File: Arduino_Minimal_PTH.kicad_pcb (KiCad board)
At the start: 2 copper layers, 27.9 x 45.7 mm, 22 parts, among them IC1 ATMEGA328P-PU, P1 I/O lo, P2 FTDI Basic, P3 A4 A5, P4 I/O hi, SW1 Reset, U1 L4931CZ50-AP, X1 CSTLS16M0X53-B0

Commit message: Placed.
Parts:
- removed C1: 10u, mfk-CRP_5.0_2.0_0.5
- removed C3: 100n, mfk-C_4.0_2.5_2.5_0.5
- removed D1, D2: LED, LED-3MM
- removed R1: 10K, mfk-R_0.25W_RN55_vert
- removed R3: 330, mfk-R_0.25W_RN55_vert
- removed R4, R5: opt, mfk-R_0.25W_RN55_vert
- removed U1: L4931CZ50-AP, mfk-TO-92_f321
- removed VAL: REF, oshw-logo-150mil-FSilk
- C2: footprint mfk-CRP_5.0_2.0_0.5 -> mfk-CRP_4.0_2.5_0.5
- C4, C7, C8: moved to B.Cu
- SW1: footprint mfk-SW_PUSH_6MM -> mfk-SW_PUSH_6x3.5mm
- moved X1 26.2 mm to (129.2, 88.1)
- moved P3 14.2 mm to (143.5, 91.4)
- moved R2 12.9 mm to (133.6, 86.4), turned to 0 degrees
- moved C4 12.0 mm to (137.8, 86.4)
- moved SW1 9.47 mm to (135.8, 89.4)
- moved C7 7.62 mm to (135.9, 110.5), turned to 180 degrees
- moved C8 7.62 mm to (135.9, 108.0), turned to 0 degrees
- moved P1 5.08 mm to (128.3, 109.2)
- moved P4 5.08 mm to (143.5, 109.2)
- moved C2 4.36 mm to (142.4, 86.4), turned to 180 degrees
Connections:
- P4 pad 1: RAW -> (no net)
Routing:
- net GND: track 106.3 -> 0.00 mm, vias 1 -> 0
- net VCC: track 75.8 -> 0.00 mm, vias 1 -> 0
- net RESET: track 44.5 -> 0.00 mm
- net A3: track 37.1 -> 0.00 mm
- net TXO: track 32.9 -> 0.00 mm
- net RXI: track 24.9 -> 0.00 mm
- net DTR: track 18.1 -> 0.00 mm
- net D9: track 17.6 -> 0.00 mm
- net A2: track 14.2 -> 0.00 mm
- net A5: track 13.9 -> 0.00 mm
- net A4: track 13.9 -> 0.00 mm
- net A1: track 12.9 -> 0.00 mm
- net A0: track 12.2 -> 0.00 mm
- net D4: track 11.2 -> 0.00 mm
- net D6: track 11.0 -> 0.00 mm
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- removed copper zone on B.Cu, net GND
- removed copper zone on F.Cu, net GND
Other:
- board size 27.9 x 45.7 mm -> 17.8 x 45.7 mm
- board text added: "NC"
- board text added: "VCC"
- board text removed: "RAW"
- board text removed: "Reset"

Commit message: Routed
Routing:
- net GND: track 0.00 -> 71.8 mm
- net VCC: track 0.00 -> 62.8 mm, vias 0 -> 1
- net RESET: track 0.00 -> 36.4 mm
- net TXO: track 0.00 -> 30.9 mm, vias 0 -> 3
- net N-0000015: track 0.00 -> 28.6 mm
- net N-000005: track 0.00 -> 26.1 mm
- net RXI: track 0.00 -> 20.1 mm
- net D9: track 0.00 -> 12.5 mm
- net A0: track 0.00 -> 10.8 mm
- net A2: track 0.00 -> 9.20 mm
- net A1: track 0.00 -> 9.20 mm
- net A3: track 0.00 -> 9.20 mm
- net D6: track 0.00 -> 6.66 mm
- net D3: track 0.00 -> 6.66 mm
- net D8: track 0.00 -> 6.66 mm
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
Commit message: Rerouted.
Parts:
- added VAL: REF, oshw-logo-100mil-FSilk, F.Cu at (129.3, 125.6)
- C4: moved to F.Cu
- moved R2 6.16 mm to (139.7, 87.2), turned to 300 degrees
- moved C4 2.93 mm to (134.9, 86.1)
- moved SW1 0.89 mm to (134.9, 89.4)
- moved C2 0.13 mm to (142.5, 86.4), turned to 270 degrees
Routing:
- net VCC: track 62.8 -> 59.0 mm, vias 1 -> 0
- net RESET: track 36.4 -> 39.7 mm
- net TXO: track 30.9 -> 27.8 mm, vias 3 -> 0
- net GND: track 71.8 -> 74.5 mm
- net DTR: track 5.13 -> 7.59 mm
- net N-000005: track 26.1 -> 28.2 mm
- net A0: track 10.8 -> 9.20 mm
- net N-0000015: track 28.6 -> 29.5 mm
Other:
- board text added: "Minimal PTH Arduino-compatible"
- board text removed: "ProMiniPTH"
- board text removed: "Vcc"

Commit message: Flooded.
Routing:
- added copper zone on B.Cu, net GND
- added copper zone on F.Cu, net GND
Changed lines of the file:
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@@
   (segment (start 135.89 109.1997) (end 135.89 110.8501) (width 0.254) (layer B.Cu) (net 27))
   (segment (start 134.6403 107.95) (end 135.89 109.1997) (width 0.254) (layer B.Cu) (net 27))
+  (zone (net 17) (net_name GND) (layer F.Cu) (hatch edge 0.508)
+    (connect_pads (clearance 0.508))
+    (min_thickness 0.2032)
+    (fill (arc_segments 16) (thermal_gap 0.508) (thermal_bridge_width 0.254))
+    (polygon
+      (pts
+        (xy 144.78 127) (xy 127 127) (xy 127 81.28) (xy 144.78 81.28)
+      )
+    )
+  )
+  (zone (net 17) (net_name GND) (layer B.Cu) (hatch edge 0.508)
+    (connect_pads (clearance 0.508))
+    (min_thickness 0.2032)
+    (fill (arc_segments 16) (thermal_gap 0.508) (thermal_bridge_width 0.254))
+    (polygon
+      (pts
+        (xy 144.78 127) (xy 127 127) (xy 127 81.28) (xy 144.78 81.28)
+      )
+    )
+  )
 )

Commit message: Silkscreen optimizations.
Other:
- board text added: "Arduino-compatible Minimal PTH"
- board text removed: "Minimal PTH Arduino-compatible"
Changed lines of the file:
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@@
     (links 47)
     (no_connects 0)
-    (area 124.553134 75.1078 156.260715 137.895001)
+    (area 122.54049 75.1078 156.260715 132.24)
     (thickness 1.6)
     (drawings 40)
@@
     (descr "Non-polar capacitor, 4.0x2.5mm, 2.5mm space, 0.5mm lead")
     (tags "capacitor non-polar bipolar")
-    (fp_text reference C7 (at 0 0 180) (layer B.SilkS)
+    (fp_text reference C7 (at 0 -2.413 180) (layer B.SilkS)
       (effects (font (size 1.524 1.524) (thickness 0.1524)) (justify mirror))
     )
@@
     (descr "Non-polar capacitor, 4.0x2.5mm, 2.5mm space, 0.5mm lead")
     (tags "capacitor non-polar bipolar")
-    (fp_text reference C8 (at 0 0) (layer B.SilkS)
+    (fp_text reference C8 (at 0 -2.159) (layer B.SilkS)
       (effects (font (size 1.524 1.524) (thickness 0.1524)) (justify mirror))
     )
@@
       (xy 0.98552 -0.31496)) (layer F.SilkS) (width 0.00254))
   )
-  (gr_text "Minimal PTH\nArduino-compatible" (at 135.128 112.649 90) (layer B.SilkS)
-    (effects (font (size 1.016 0.889) (thickness 0.2032)) (justify left mirror))
-  )
-  (gr_circle (center 130.302 92.71) (end 130.302 92.456) (layer F.SilkS) (width 0.254))
+  (gr_circle (center 130.302 92.71) (end 130.556 92.71) (layer F.SilkS) (width 0.254))
+  (gr_text "Arduino-compatible\nMinimal PTH\n" (at 135.255 91.44 90) (layer B.SilkS)
+    (effects (font (size 1.27 0.8382) (thickness 0.2032)) (justify left mirror))
+  )
   (gr_text A5 (at 141.732 91.313 90) (layer F.SilkS)
     (effects (font (size 0.635 0.762) (thickness 0.1524)))

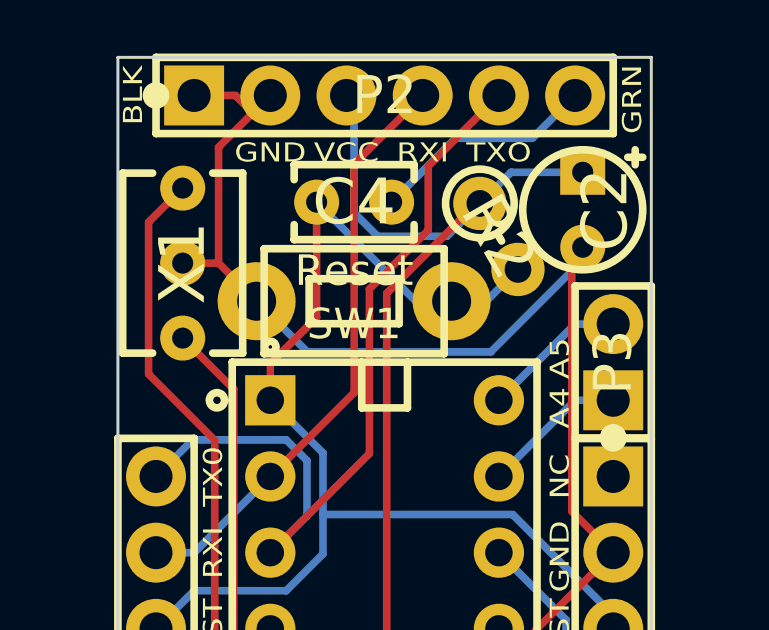
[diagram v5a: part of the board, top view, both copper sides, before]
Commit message: Silkscreen tweaks.
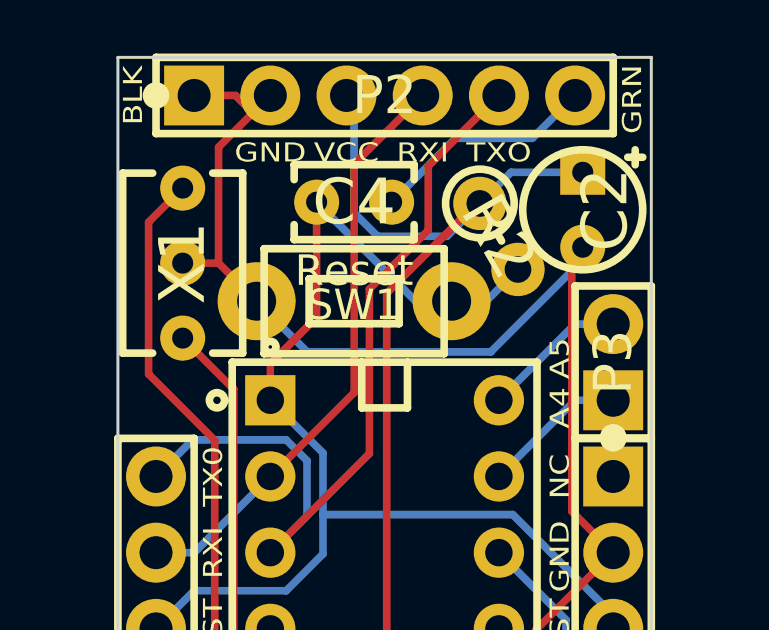
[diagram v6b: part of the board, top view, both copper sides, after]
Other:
- board text added: "Arduino compatible Minimal PTH"
- board text removed: "Arduino-compatible Minimal PTH"
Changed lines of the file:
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@@
   )
   (layers
-    (15 F.Cu signal)
-    (0 B.Cu signal)
+    (15 F.Cu signal hide)
+    (0 B.Cu signal hide)
     (20 B.SilkS user)
-    (21 F.SilkS user)
+    (21 F.SilkS user hide)
     (22 B.Mask user)
     (23 F.Mask user)
@@
   (module mfk-SW_PUSH_6x3.5mm (layer F.Cu)
     (at 134.874 89.408 180)
-    (fp_text reference SW1 (at 0 -0.762 180) (layer F.SilkS)
+    (fp_text reference SW1 (at 0 -0.127 180) (layer F.SilkS)
       (effects (font (size 1.016 1.016) (thickness 0.2032)))
     )
@@
   )
   (gr_circle (center 130.302 92.71) (end 130.556 92.71) (layer F.SilkS) (width 0.254))
-  (gr_text "Arduino-compatible\nMinimal PTH\n" (at 135.255 91.44 90) (layer B.SilkS)
+  (gr_text "Arduino compatible\nMinimal PTH\n" (at 135.255 91.186 90) (layer B.SilkS)
     (effects (font (size 1.27 0.8382) (thickness 0.2032)) (justify left mirror))
   )
